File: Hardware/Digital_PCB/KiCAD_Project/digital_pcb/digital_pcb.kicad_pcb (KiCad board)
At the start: 4 copper layers, 75 x 84.8 mm, 99 parts, among them J1 Conn_01x02, J2 ISP, J3 Conn_01x02, J4 Board to Board, J5 Spare 1, J6 Power, J7 Power Switch, Q1 MMBT3904, U1 STM32F103CBTx, U10 TPS793, U11 TPS1H000, U2 BNO055, U3 HTU21D, U4 ADS1220, U5 KC2520B-C2, U6 SN74LVC1G17-EP, U7 LT1521-3.3, U8 TEC 2-0921, U9 TPS723, Y1 8MHz, Y2 32.768kHz

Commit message: Update for Rev 3.0
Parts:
- removed R34: 470k, Resistor_SMD:R_0603_1608Metric_Pad1.05x0.95mm_HandSolder
- removed R35: 10k, Resistor_SMD:R_0603_1608Metric_Pad1.05x0.95mm_HandSolder
- removed the U3 at (165.2, 80.8)
- removed the U9 at (139.2, 73.8)
- added C36: 10n, Capacitor_SMD:C_0603_1608Metric, F.Cu at (139.2, 67.8)
- added PCB1: barepcb, lib_fp:barepcb, F.Cu at (110.0, 55.9)
- added U2: BME280, Package_LGA:Bosch_LGA-8_2.5x2.5mm_P0.65mm_ClockwisePinNumbering, F.Cu at (165.4, 81.7)
- added U8: TPS723, Package_TO_SOT_SMD:SOT-23-5_HandSoldering, F.Cu at (139.2, 73.8)
- C1: value 1u -> 0.1u; footprint Capacitors_SMD:C_0603_HandSoldering -> Capacitor_SMD:C_0603_1608Metric
- C10, C12, C20, C4, C8, C9: footprint Capacitors_SMD:C_0603_HandSoldering -> Capacitor_SMD:C_0603_1608Metric
- C11: value 22pF -> 0.1u; footprint Capacitors_SMD:C_0603_HandSoldering -> Capacitor_SMD:C_0603_1608Metric
- C13: value 0.1u -> 22pF; footprint Capacitors_SMD:C_0603_HandSoldering -> Capacitor_SMD:C_0603_1608Metric
- C14, C15, C16: value NP -> 0.1u; footprint Capacitors_SMD:C_0603_HandSoldering -> Capacitor_SMD:C_0603_1608Metric
- C17, C18: value 0.1u -> NP; footprint Capacitors_SMD:C_0603_HandSoldering -> Capacitor_SMD:C_0603_1608Metric
- C19: value 0.01u -> NP; footprint Capacitors_SMD:C_0603_HandSoldering -> Capacitor_SMD:C_0603_1608Metric
- C2, C3: value 20pF -> 0.1u; footprint Capacitors_SMD:C_0603_HandSoldering -> Capacitor_SMD:C_0603_1608Metric
- C21: value 0.1u -> 0.01u; footprint Capacitors_SMD:C_0603_HandSoldering -> Capacitor_SMD:C_0603_1608Metric
- C22, C35: footprint Capacitor_SMD:C_0805_2012Metric_Pad1.15x1.40mm_HandSolder -> Capacitor_SMD:C_0805_2012Metric
- C23, C34: value 10u -> 0.1u; footprint Capacitors_SMD:C_0805_HandSoldering -> Capacitor_SMD:C_0603_1608Metric
- C24, C27: value 1u -> 10u; footprint Capacitors_SMD:C_0603_HandSoldering -> Capacitor_SMD:C_0805_2012Metric
- C25: value 0.1u -> 2.2u; footprint Capacitors_SMD:C_0603_HandSoldering -> Capacitor_SMD:C_0603_1608Metric
- C26: value 10u -> 2.2u; footprint Capacitors_SMD:C_0805_HandSoldering -> Capacitor_SMD:C_0603_1608Metric
- C28, C6: value 0.1u -> 1u; footprint Capacitors_SMD:C_0603_HandSoldering -> Capacitor_SMD:C_0603_1608Metric
- C29: value 2.2u -> 0.1u; footprint Capacitors_SMD:C_0603_HandSoldering -> Capacitor_SMD:C_0603_1608Metric
- C30: value 0.1u -> 10u; footprint Capacitors_SMD:C_0603_HandSoldering -> Capacitor_SMD:C_0805_2012Metric
- C31: value 10n -> 1u; footprint Capacitors_SMD:C_0603_HandSoldering -> Capacitor_SMD:C_0603_1608Metric
- C32: value 10n -> 0.1u; footprint Capacitors_SMD:C_0603_HandSoldering -> Capacitor_SMD:C_0603_1608Metric
- C33: value 2.2u -> 10n; footprint Capacitors_SMD:C_0603_HandSoldering -> Capacitor_SMD:C_0603_1608Metric
- C5, C7: value 0.1u -> 20pF; footprint Capacitors_SMD:C_0603_HandSoldering -> Capacitor_SMD:C_0603_1608Metric
- J1, J3: footprint Pin_Headers:Pin_Header_Straight_1x02_Pitch2.54mm -> Connector_PinHeader_2.54mm:PinHeader_1x02_P2.54mm_Vertical
- J2: footprint Pin_Headers:Pin_Header_Straight_1x04_Pitch2.54mm -> Connector_PinHeader_2.54mm:PinHeader_1x04_P2.54mm_Vertical
- J4: value Board to Board -> Spare 1; footprint Pin_Headers:Pin_Header_Straight_1x10_Pitch2.54mm -> Connector_PinHeader_2.54mm:PinHeader_1x04_P2.54mm_Vertical
- J5: value Spare 1 -> Board to Board; footprint Pin_Headers:Pin_Header_Straight_1x04_Pitch2.54mm -> Connector_PinHeader_2.54mm:PinHeader_1x10_P2.54mm_Vertical
- J6: value Power -> Power Switch; footprint Pin_Headers:Pin_Header_Straight_1x02_Pitch2.54mm -> Connector_PinHeader_2.54mm:PinHeader_1x02_P2.54mm_Vertical
- J7: value Power Switch -> Power; footprint Pin_Headers:Pin_Header_Straight_1x02_Pitch2.54mm -> Connector_PinHeader_2.54mm:PinHeader_1x02_P2.54mm_Vertical
- R1, R2: value 100k -> NP; footprint Resistors_SMD:R_0603_HandSoldering -> Resistor_SMD:R_0603_1608Metric
- R10, R11, R12, R13, R14, R15, R17, R19, R22, R23, R24, R8, R9: footprint Resistors_SMD:R_0603_HandSoldering -> Resistor_SMD:R_0603_1608Metric
- R16: value NP -> 10k; footprint Resistors_SMD:R_0603_HandSoldering -> Resistor_SMD:R_0603_1608Metric
- R18, R27: value 10k -> NP; footprint Resistors_SMD:R_0603_HandSoldering -> Resistor_SMD:R_0603_1608Metric
- R20, R6: value NP -> 0R0; footprint Resistors_SMD:R_0603_HandSoldering -> Resistor_SMD:R_0603_1608Metric
- R21, R5: value 10k -> 0R0; footprint Resistors_SMD:R_0603_HandSoldering -> Resistor_SMD:R_0603_1608Metric
- R25, R7: value 0R0 -> 10k; footprint Resistors_SMD:R_0603_HandSoldering -> Resistor_SMD:R_0603_1608Metric
- R26: value 0R0 -> NP; footprint Resistors_SMD:R_0603_HandSoldering -> Resistor_SMD:R_0603_1608Metric
- R28: value NP -> 165; footprint Resistors_SMD:R_0603_HandSoldering -> Resistor_SMD:R_1206_3216Metric
- R29: value NP -> 3.9k; footprint Resistors_SMD:R_0603_HandSoldering -> Resistor_SMD:R_0603_1608Metric
- R3: value NP -> 100k; footprint Resistors_SMD:R_0603_HandSoldering -> Resistor_SMD:R_0603_1608Metric
- R30: value 3.9k -> 33k; footprint Resistors_SMD:R_0603_HandSoldering -> Resistor_SMD:R_0603_1608Metric
- R31: value 33k -> 0R0; footprint Resistors_SMD:R_0603_HandSoldering -> Resistor_SMD:R_0603_1608Metric
- R32: value 165 -> 470k; footprint Resistor_SMD:R_1206_3216Metric_Pad1.42x1.75mm_HandSolder -> Resistor_SMD:R_0603_1608Metric
- R33: value 0R0 -> 10k; footprint Resistor_SMD:R_0603_1608Metric_Pad1.05x0.95mm_HandSolder -> Resistor_SMD:R_0603_1608Metric
- R4: value 0R0 -> 100k; footprint Resistors_SMD:R_0603_HandSoldering -> Resistor_SMD:R_0603_1608Metric
- moved J4 75.2 mm to (180.1, 99.8), turned to 180 degrees
- moved J5 75.2 mm to (118.7, 56.4), turned to 0 degrees
- moved C23 49.6 mm to (186.3, 76.6), turned to 180 degrees
- moved R29 49.3 mm to (183.5, 73.3), turned to 270 degrees
- moved C21 45.5 mm to (151.8, 106.2)
- moved R28 45.1 mm to (169.8, 70.1), turned to 270 degrees
- moved R31 38.5 mm to (146.7, 57.7)
- moved R19 37.3 mm to (151.6, 118.4), turned to 180 degrees
- moved R20 36.1 mm to (159.8, 119.4), turned to 270 degrees
- moved C14 35.6 mm to (154.7, 84.5)
- moved R32 31.0 mm to (142.1, 56.3), turned to 0 degrees
- moved C24 27.2 mm to (136.4, 56.9), turned to 180 degrees
- moved R7 25.4 mm to (151.1, 88.4), turned to 0 degrees
- moved C1 22.5 mm to (173.5, 92.3)
- moved C5 21.5 mm to (156.3, 88.5)
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- renumbered U8 to U11, U2 to U3, U11 to U7, U7 to U9
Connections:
- C1 pad 1: GND -> +3V3
- C1 pad 2: /Reset -> GND
- C10 pad 1: Net-(C10-Pad1) -> +3V3
- C11 pad 1: GND -> +3V3
- C11 pad 2: Net-(C11-Pad2) -> GND
- C13 pad 1: +3V3 -> GND
- C13 pad 2: GND -> Net-(C13-Pad2)
- C15 pad 1: Net-(C15-Pad1) -> +3V3
- C16 pad 1: Net-(C14-Pad1) -> +2V5
- C16 pad 2: Net-(C15-Pad1) -> GND
- C17 pad 1: +3V3 -> Net-(C17-Pad1)
- C18 pad 1: -2V5 -> Net-(C17-Pad1)
- C18 pad 2: GND -> Net-(C18-Pad2)
- C19 pad 1: +3V3 -> Net-(C18-Pad2)
- C2 pad 1: Net-(C2-Pad1) -> +3V3
- C20 pad 1: +2V5 -> -2V5
- C23 pad 1: +BATT -> +3V3
- C24 pad 1: +BATT -> Net-(C24-Pad1)
- C25 pad 1: +BATT -> -5V
- C26 pad 1: +3V3 -> -2V5
- C27 pad 1: +3V3 -> +BATT
- C28 pad 1: +3V3 -> +BATT
- C29 pad 1: -5V -> +BATT
- C3 pad 1: Net-(C3-Pad1) -> +3V3
- C30 pad 1: +5V -> +3V3
- C31 pad 1: Net-(C31-Pad1) -> +3V3
- C32 pad 1: Net-(C32-Pad1) -> +3V3
- C33 pad 1: -2V5 -> Net-(C33-Pad1)
- C34 pad 1: +2V5 -> +5V
- C35 pad 1: Net-(C35-Pad1) -> +2V5
- C5 pad 1: +3V3 -> Net-(C5-Pad1)
- C6 pad 1: +3V3 -> GND
- C6 pad 2: GND -> /Reset
- C7 pad 1: +3V3 -> Net-(C7-Pad1)
- J4 pad 1: GND -> Net-(J4-Pad1)
- J4 pad 2: +5V -> Net-(J4-Pad2)
- J4 pad 3: -5V -> Net-(J4-Pad3)
- J4 pad 4: AMP_IN -> Net-(J4-Pad4)
- J5 pad 1: Net-(J5-Pad1) -> GND
- J5 pad 2: Net-(J5-Pad2) -> +5V
- J5 pad 3: Net-(J5-Pad3) -> -5V
- J5 pad 4: Net-(J5-Pad4) -> AMP_IN
- J6 pad 1: GND -> Net-(F1-Pad1)
- J6 pad 2: Net-(F1-Pad2) -> Net-(J6-Pad2)
- J7 pad 1: Net-(F1-Pad1) -> GND
- J7 pad 2: Net-(J7-Pad2) -> Net-(F1-Pad2)
- R1 pad 1: Net-(R1-Pad1) -> +3V3
- R1 pad 2: /Boot0 -> Net-(R1-Pad2)
- R16 pad 1: /Peripherals/BNO_ADDR -> GND
- R16 pad 2: +3V3 -> Net-(R16-Pad2)
- R17 pad 2: /Peripherals/BNO_ADDR -> Net-(R17-Pad2)
- R18 pad 1: GND -> IMU_INT
- R18 pad 2: Net-(R18-Pad2) -> +3V3
- R19 pad 1: GND -> Net-(R19-Pad1)
- R19 pad 2: Net-(R19-Pad2) -> AMP_OUT
- R2 pad 1: Net-(R2-Pad1) -> +3V3
- R2 pad 2: /Boot1 -> Net-(R2-Pad2)
- R20 pad 1: IMU_INT -> Net-(C17-Pad1)
- R20 pad 2: +3V3 -> Net-(R19-Pad1)
- R21 pad 2: AMP_OUT -> Net-(C17-Pad1)
- R22 pad 2: Net-(R21-Pad1) -> Net-(R19-Pad1)
- R23 pad 1: Net-(C14-Pad1) -> Net-(R23-Pad1)
- R23 pad 2: Net-(R21-Pad1) -> Net-(C18-Pad2)
- R24 pad 1: Net-(C15-Pad1) -> Net-(C18-Pad2)
- R25 pad 2: Net-(C14-Pad1) -> +3V3
- R26 pad 1: Net-(R26-Pad1) -> Net-(R25-Pad1)
- R26 pad 2: Net-(C15-Pad1) -> GND
- R27 pad 1: Net-(R27-Pad1) -> GND
- R27 pad 2: +3V3 -> Net-(R27-Pad2)
- R28 pad 1: Net-(R27-Pad1) -> Net-(D1-Pad2)
- R28 pad 2: GND -> +5V
- R29 pad 1: GND -> Net-(Q1-Pad1)
- R3 pad 1: +3V3 -> Net-(R1-Pad2)
- R3 pad 2: Net-(R1-Pad1) -> /Boot0
- R30 pad 1: Net-(Q1-Pad1) -> GND
- R30 pad 2: Net-(R30-Pad2) -> Net-(Q1-Pad1)
- R31 pad 1: GND -> +BATT
- R31 pad 2: Net-(Q1-Pad1) -> Net-(J6-Pad2)
- R32 pad 1: Net-(D1-Pad2) -> Net-(C24-Pad1)
- R32 pad 2: +5V -> Net-(J6-Pad2)
- R33 pad 1: +BATT -> Net-(R33-Pad1)
- R33 pad 2: Net-(J7-Pad2) -> GND
- R4 pad 1: Net-(R1-Pad1) -> Net-(R2-Pad2)
- R4 pad 2: GND -> /Boot1
- R5 pad 1: +3V3 -> Net-(R1-Pad2)
- R5 pad 2: /Reset -> GND
- R6 pad 1: +3V3 -> Net-(R2-Pad2)
- R6 pad 2: Net-(R2-Pad1) -> GND
- R7 pad 1: Net-(R2-Pad1) -> +3V3
- R7 pad 2: GND -> /Reset
- R8 pad 1: Net-(C2-Pad1) -> Net-(C5-Pad1)
- R8 pad 2: Net-(C3-Pad1) -> Net-(C7-Pad1)
- U1 pad 1: Net-(U1-Pad1) -> (no net)
- U1 pad 10: Net-(U1-Pad10) -> (no net)
- U1 pad 11: Net-(U1-Pad11) -> (no net)
- U1 pad 12: Net-(U1-Pad12) -> (no net)
- U1 pad 18: Net-(U1-Pad18) -> (no net)
- U1 pad 2: Net-(U1-Pad2) -> (no net)
- U1 pad 20: Net-(U1-Pad20) -> (no net)
- U1 pad 21: Net-(U1-Pad21) -> (no net)
- U1 pad 22: Net-(U1-Pad22) -> (no net)
- U1 pad 25: Net-(J5-Pad1) -> Net-(J4-Pad1)
- U1 pad 26: Net-(J5-Pad2) -> Net-(J4-Pad2)
- U1 pad 27: Net-(J5-Pad3) -> Net-(J4-Pad3)
- U1 pad 28: Net-(J5-Pad4) -> Net-(J4-Pad4)
- U1 pad 29: Net-(U1-Pad29) -> (no net)
- U1 pad 3: Net-(U1-Pad3) -> (no net)
- U1 pad 31: UART1_RX -> (no net)
- U1 pad 32: Net-(U1-Pad32) -> (no net)
- U1 pad 33: Net-(U1-Pad33) -> (no net)
- U1 pad 38: Net-(U1-Pad38) -> (no net)
- U1 pad 39: Net-(U1-Pad39) -> (no net)
- U1 pad 4: Net-(U1-Pad4) -> (no net)
- U1 pad 40: Net-(U1-Pad40) -> (no net)
- U1 pad 45: Net-(U1-Pad45) -> (no net)
- U1 pad 46: Net-(U1-Pad46) -> (no net)
- U1 pad 5: Net-(C2-Pad1) -> Net-(C5-Pad1)
- U1 pad 6: Net-(C3-Pad1) -> Net-(C7-Pad1)
- U10 pad 4: Net-(C32-Pad1) -> Net-(C36-Pad1)
- U11 pad 3: Net-(U8-Pad3) -> (no net)
- U11 pad 5: Net-(U8-Pad5) -> (no net)
- U3 pad 1: Net-(U2-Pad1) -> (no net)
- U3 pad 11: Net-(U2-Pad11) -> (no net)
- U3 pad 12: Net-(U2-Pad12) -> (no net)
- U3 pad 13: Net-(U2-Pad13) -> (no net)
- U3 pad 17: /Peripherals/BNO_ADDR -> GND
- U3 pad 21: Net-(U2-Pad21) -> (no net)
- U3 pad 22: Net-(U2-Pad22) -> (no net)
- U3 pad 23: Net-(U2-Pad23) -> (no net)
- U3 pad 24: Net-(U2-Pad24) -> (no net)
- U3 pad 26: Net-(C11-Pad2) -> Net-(C12-Pad2)
- U3 pad 27: Net-(C12-Pad2) -> Net-(C13-Pad2)
- U3 pad 5: Net-(R19-Pad2) -> Net-(R17-Pad2)
- U3 pad 6: Net-(R18-Pad2) -> Net-(R16-Pad2)
- U3 pad 7: Net-(U2-Pad7) -> (no net)
- U3 pad 8: Net-(U2-Pad8) -> (no net)
- U3 pad 9: Net-(C10-Pad1) -> Net-(C14-Pad1)
- U4 pad 10: Net-(R25-Pad1) -> Net-(R21-Pad1)
- U4 pad 11: Net-(U4-Pad11) -> (no net)
- U4 pad 3: Net-(R29-Pad2) -> Net-(R27-Pad2)
- U4 pad 6: Net-(U4-Pad6) -> (no net)
- U4 pad 7: Net-(R26-Pad1) -> Net-(R23-Pad1)
- U4 pad 8: Net-(U4-Pad8) -> (no net)
- U4 pad 9: Net-(U4-Pad9) -> (no net)
- U5 pad 1: Net-(R27-Pad1) -> Net-(R25-Pad1)
- U5 pad 3: Net-(R29-Pad2) -> Net-(R27-Pad2)
- U6 pad 1: Net-(U6-Pad1) -> (no net)
- U6 pad 4: Net-(R30-Pad2) -> Net-(R29-Pad2)
- U7 pad 1: Net-(C35-Pad1) -> Net-(C24-Pad1)
- U7 pad 2: Net-(R35-Pad1) -> Net-(R33-Pad1)
- U7 pad 3: Net-(U11-Pad3) -> (no net)
- U7 pad 8: Net-(J7-Pad2) -> Net-(J6-Pad2)
- Y1 pad 1: Net-(C2-Pad1) -> Net-(C5-Pad1)
- Y1 pad 2: Net-(C3-Pad1) -> Net-(C7-Pad1)
- Y2 pad 1: Net-(C11-Pad2) -> Net-(C12-Pad2)
- Y2 pad 2: Net-(C12-Pad2) -> Net-(C13-Pad2)
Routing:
- net Net-(J7-Pad2): track 70.6 -> 0.00 mm, vias 2 -> 0
- net Net-(J6-Pad2): track 0.00 -> 70.6 mm, vias 0 -> 2
- net Net-(C5-Pad1): track 0.00 -> 16.9 mm
- net Net-(C2-Pad1): track 16.9 -> 0.00 mm
- net Net-(C7-Pad1): track 0.00 -> 16.8 mm
- net Net-(C3-Pad1): track 16.8 -> 0.00 mm
- net Net-(C13-Pad2): track 0.00 -> 16.0 mm
- net Net-(C11-Pad2): track 15.4 -> 0.00 mm
- net Net-(J5-Pad4): track 14.2 -> 0.00 mm
- net Net-(J4-Pad4): track 0.00 -> 14.2 mm
- net Net-(J5-Pad3): track 12.2 -> 0.00 mm
- net Net-(J4-Pad3): track 0.00 -> 12.2 mm
- net Net-(R19-Pad1): track 0.00 -> 11.8 mm
- net Net-(C18-Pad2): track 0.00 -> 11.0 mm
- net Net-(C15-Pad1): track 11.0 -> 0.00 mm
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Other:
- board text added: "NSSL EFM Digital Rotating Electronics Rev 3.0 P/N 3-0000069"
- board text removed: "NSSL EFM Digital Rotating Electronics Rev 2.0 -April 2020 P/N 3-0000031"

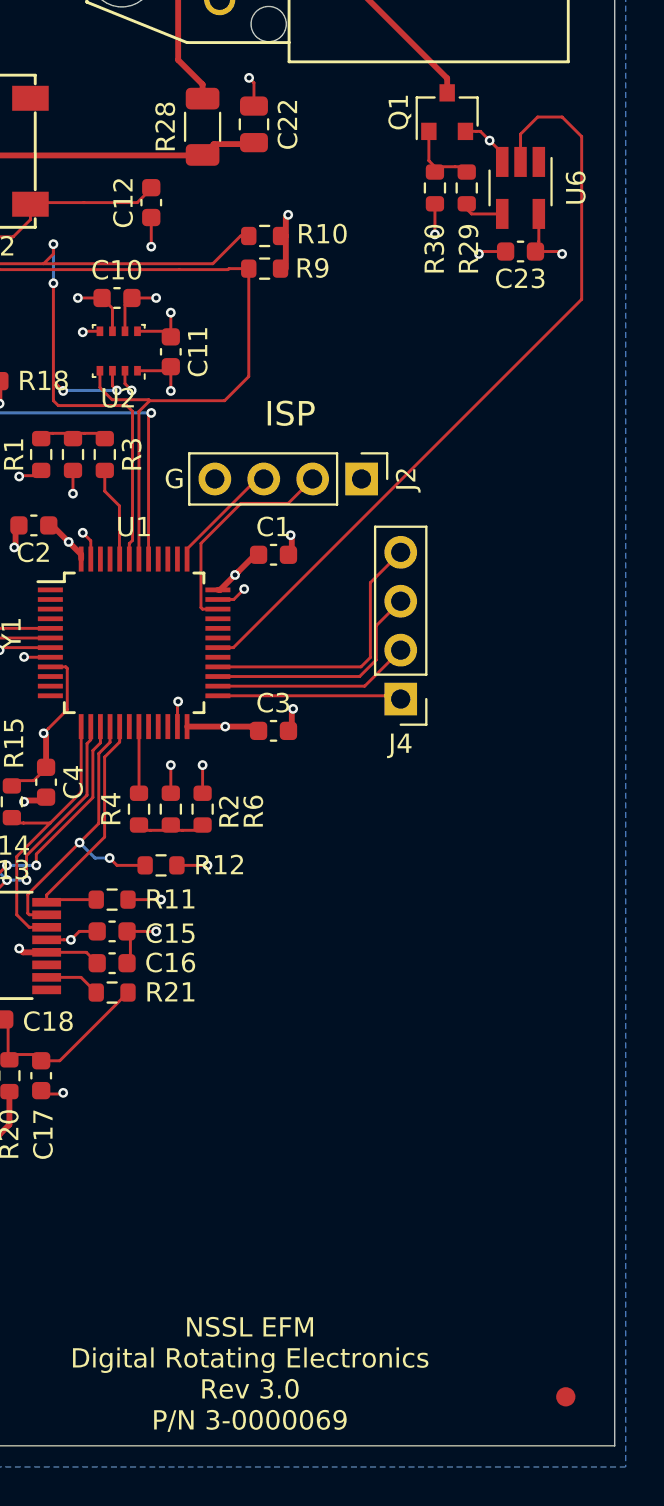
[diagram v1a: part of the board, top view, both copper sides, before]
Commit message: Add activity LED and another IMU footprint. Closes #49 #45
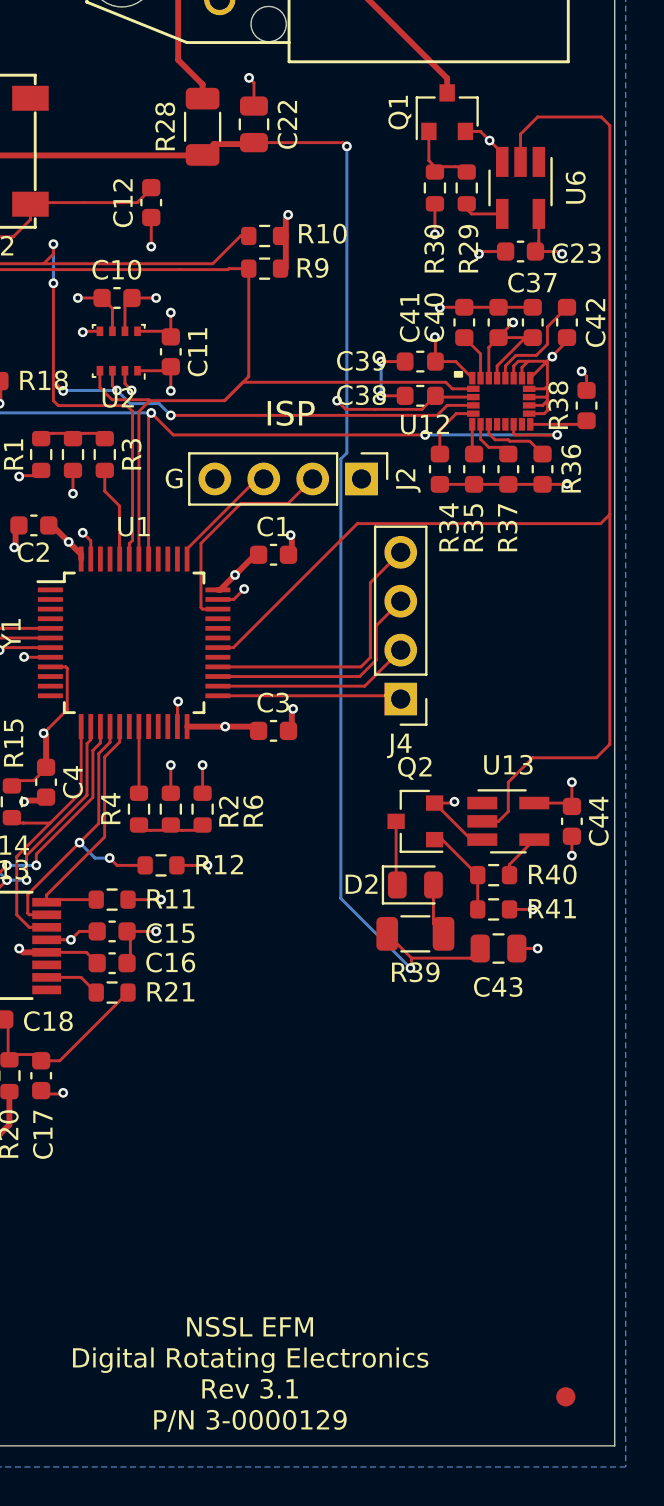
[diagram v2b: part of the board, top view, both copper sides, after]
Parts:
- added C37: 1-0000007, capacitors_0603:1-0000007, F.Cu at (186.9, 80.3)
- added C38: 1-0000007, capacitors_0603:1-0000007, F.Cu at (181.1, 84.1)
- added C39: 1-0000007, capacitors_0603:1-0000007, F.Cu at (181.1, 82.3)
- added C40: 1-0000007, capacitors_0603:1-0000007, F.Cu at (185.2, 80.3)
- added C41: 1-0000007, capacitors_0603:1-0000007, F.Cu at (183.4, 80.3)
- added C42: 1-0000014, capacitors_0603:1-0000014, F.Cu at (188.7, 80.3)
- added C43: 10u, Capacitor_SMD:C_0805_2012Metric, F.Cu at (185.2, 112.8)
- added C44: 0.1u, Capacitor_SMD:C_0603_1608Metric, F.Cu at (189.0, 106.2)
- added D2: 1-0000599, leds_0805:1-0000599, F.Cu at (180.8, 109.5)
- added Q2: 1-0000036, transistors:1-0000036, F.Cu at (180.8, 106.2)
- added R34: 1-0000010, resistors_0603:1-0000010, F.Cu at (182.1, 87.9)
- added R35: 1-0000010, resistors_0603:1-0000010, F.Cu at (183.9, 87.9)
- added R36: 1-0000010, resistors_0603:1-0000010, F.Cu at (187.5, 87.9)
- added R37: 1-0000010, resistors_0603:1-0000010, F.Cu at (185.7, 87.9)
- added R38: 1-0000006, resistors_0603:1-0000006, F.Cu at (189.7, 84.6)
- added R39: 165, Resistor_SMD:R_1206_3216Metric, F.Cu at (180.8, 112.0)
- added R40: 3.9k, Resistor_SMD:R_0603_1608Metric, F.Cu at (184.9, 109.0)
- added R41: 33k, Resistor_SMD:R_0603_1608Metric, F.Cu at (184.9, 110.7)
- added U12: 1-0000925, sensors:1-0000925, F.Cu at (185.3, 84.4)
- added U13: SN74LVC1G17-EP, Package_TO_SOT_SMD:SOT-23-5_HandSoldering, F.Cu at (185.7, 106.2)
- Q1: value MMBT3904 -> 1-0000036; footprint TO_SOT_Packages_SMD:SOT-23 -> transistors:1-0000036
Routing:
- net +5V: track 74.4 -> 129.7 mm, vias 2 -> 4
- net UART1_TX: track 40.2 -> 71.2 mm
- net +3V3: track 65.6 -> 96.0 mm, vias 22 -> 28
- net GND: track 91.5 -> 121.3 mm, vias 52 -> 60
- net IMU_INT: track 21.3 -> 45.6 mm, vias 2 -> 4
- net I2C_SDA: track 41.7 -> 60.9 mm, vias 4 -> 5
- net I2C_SCL: track 38.6 -> 52.1 mm
- net Net-(C42-Pad2): track 0.00 -> 5.62 mm
- net Net-(Q2-Pad1): track 0.00 -> 4.78 mm
- net Net-(R36-Pad2): track 0.00 -> 3.71 mm
- net Net-(R34-Pad2): track 0.00 -> 3.34 mm
- net Net-(D2-Pad1): track 0.00 -> 3.33 mm
- net Net-(R38-Pad1): track 0.00 -> 3.00 mm
- net Net-(D2-Pad2): track 0.00 -> 2.76 mm
- net Net-(R37-Pad2): track 0.00 -> 2.53 mm
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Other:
- board text added: "NSSL EFM Digital Rotating Electronics Rev 3.1 P/N 3-0000129"
- board text removed: "NSSL EFM Digital Rotating Electronics Rev 3.0 P/N 3-0000069"

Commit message: Digital PCB revs
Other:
- rule pad_to_mask_clearance: 0.0508 -> 0
